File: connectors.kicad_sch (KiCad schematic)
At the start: 9 parts, among them J1 OLED, J2 SWD, J3 OBDII

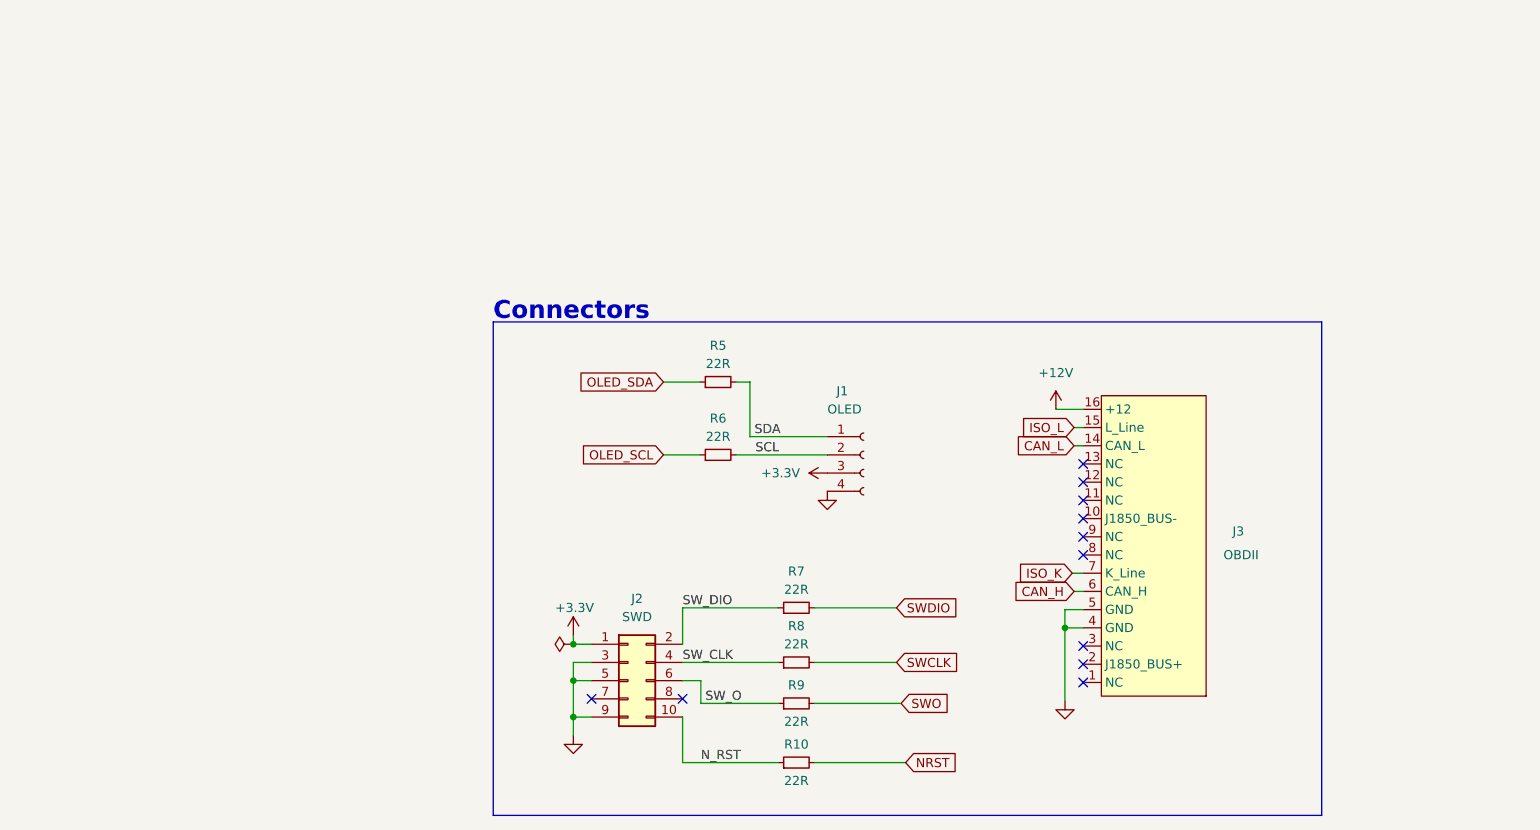
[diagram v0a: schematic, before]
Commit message: Board v2 - reduced size
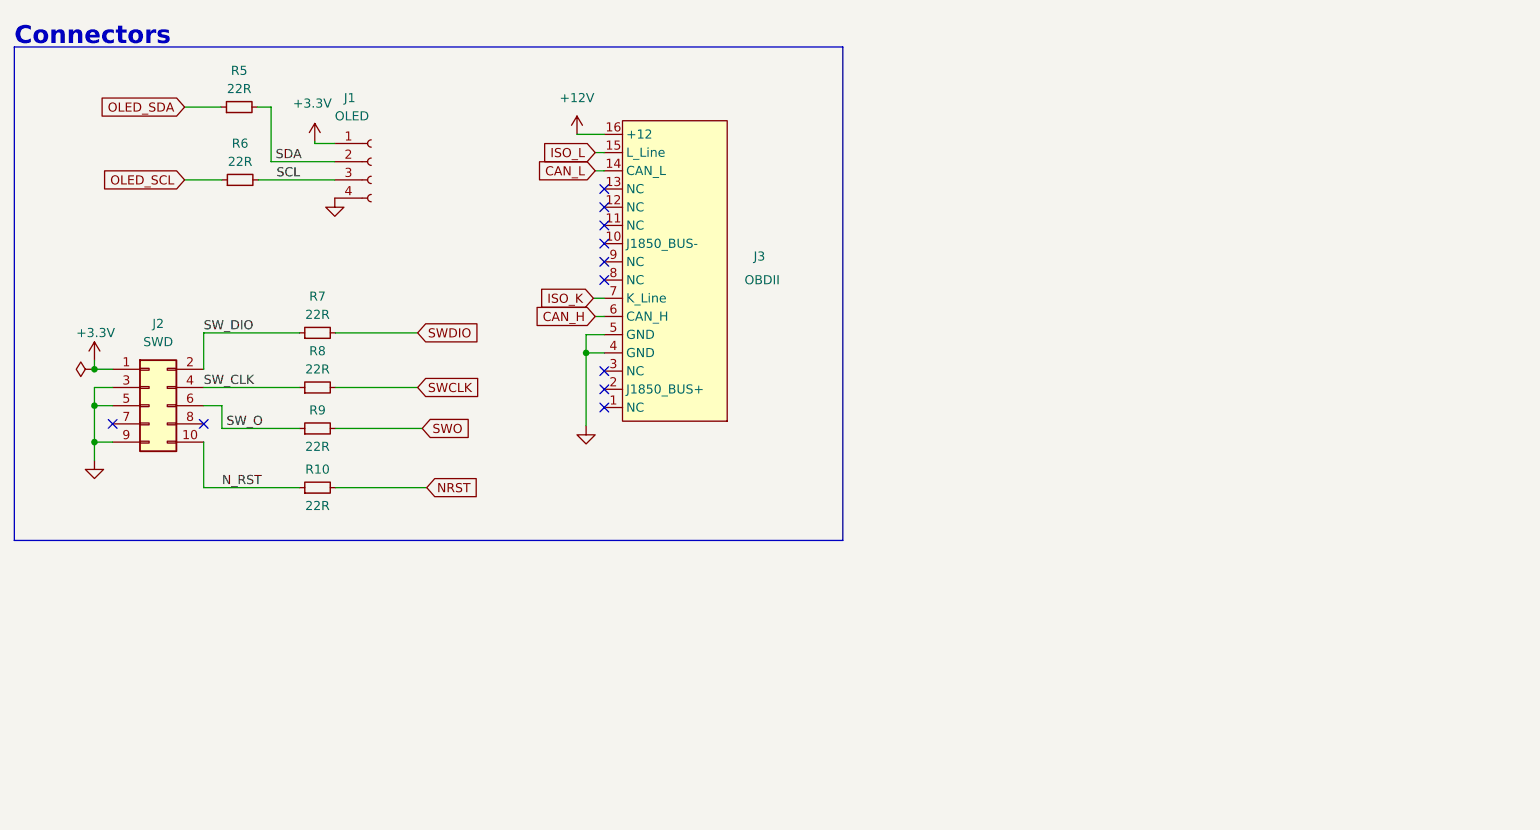
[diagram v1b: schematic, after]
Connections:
- net +3.3V: now also J1.1 (Pin_1); no longer J1.3 (Pin_3)
- net SCL: now also J1.3 (Pin_3); no longer J1.2 (Pin_2)
- net SDA: now also J1.2 (Pin_2); no longer J1.1 (Pin_1)
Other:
- moved on the sheet: J1, J2, J3, R10, R5, R6, R7, R8, R9

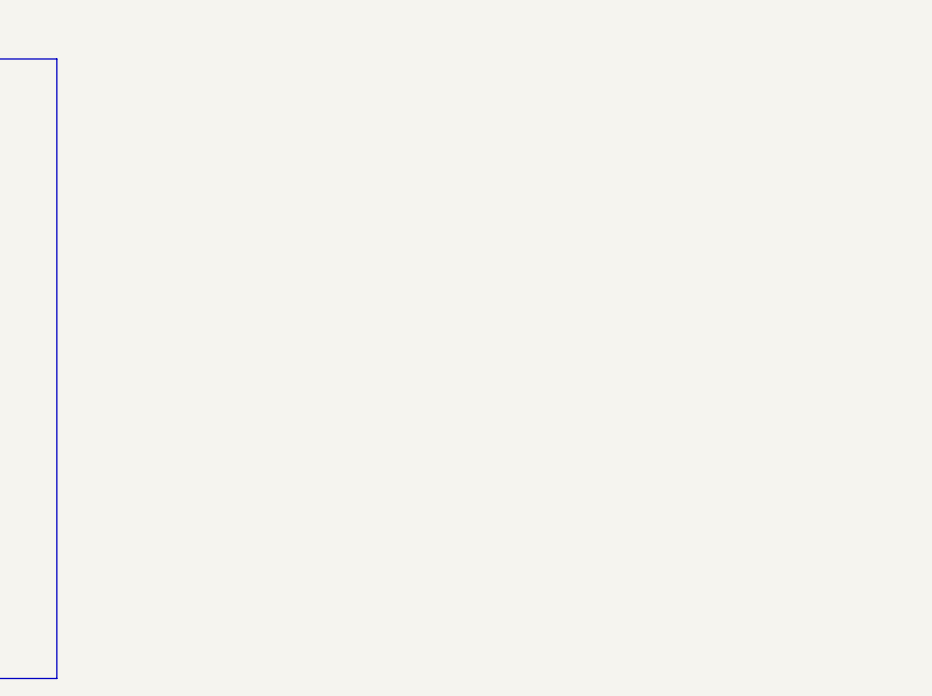
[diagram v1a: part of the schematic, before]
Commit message: Further board size reduction
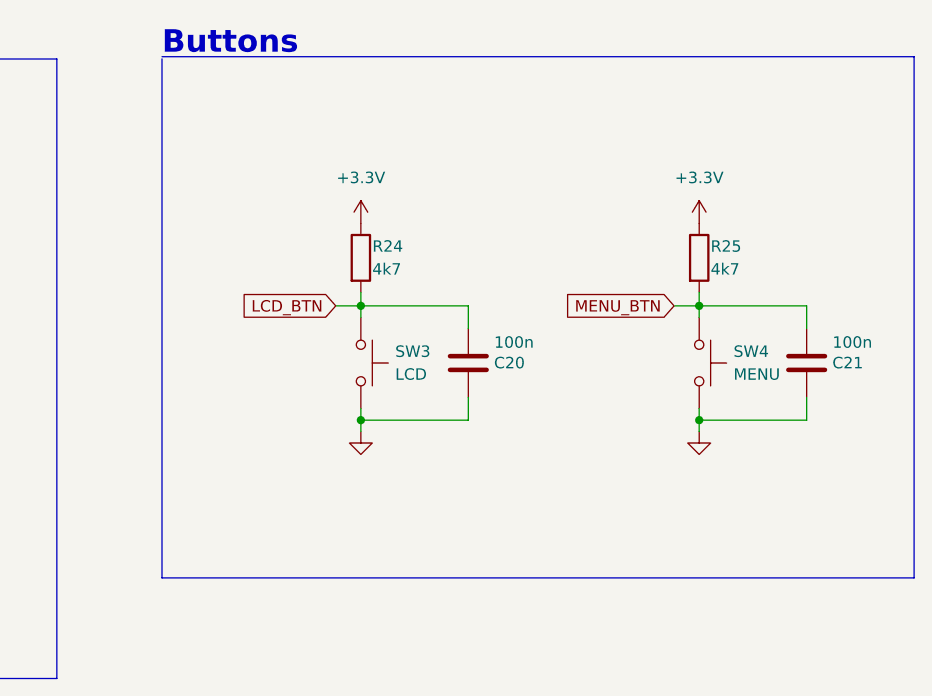
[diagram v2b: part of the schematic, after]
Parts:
- added C20, C21: 100n, Capacitor_SMD:C_0402_1005Metric, symbol Device:C
- added R24, R25: 4k7, Resistor_SMD:R_0402_1005Metric, symbol Device:R
- added SW3: LCD, Connector_PinHeader_1.27mm:PinHeader_1x02_P1.27mm_Vertical, symbol Switch:SW_Push
- added SW4: MENU, Connector_PinHeader_1.27mm:PinHeader_1x02_P1.27mm_Vertical, symbol Switch:SW_Push
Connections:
- net +3.3V: now also R24.1, R25.1
- net GND: now also C20.1, C21.1, SW3.2, SW4.2
- new net LCD_BTN: C20.2, R24.2, SW3.1
- new net MENU_BTN: C21.2, R25.2, SW4.1
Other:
- note added: "Buttons"

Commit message: KLine update 21/01/23
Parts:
- added R11: 100k, Resistor_SMD:R_0402_1005Metric, symbol Device:R_Small
- added R12, R22: 4k7, Resistor_SMD:R_0402_1005Metric, symbol Device:R
- added R23: 27k, Resistor_SMD:R_0402_1005Metric, symbol Device:R_Small
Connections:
- net +12V: now also R11.1
- net +3.3V: now also R12.1, R22.1
- net GND: now also R23.2
- net OLED_SCL: now also R12.2
- net OLED_SDA: now also R22.2
- new net BAT_V: R11.2, R23.1
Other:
- note added: "OLED Display"
- moved on the sheet: J1, J2, R10, R5, R6, R7, R8, R9
